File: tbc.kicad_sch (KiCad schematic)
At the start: 0 parts

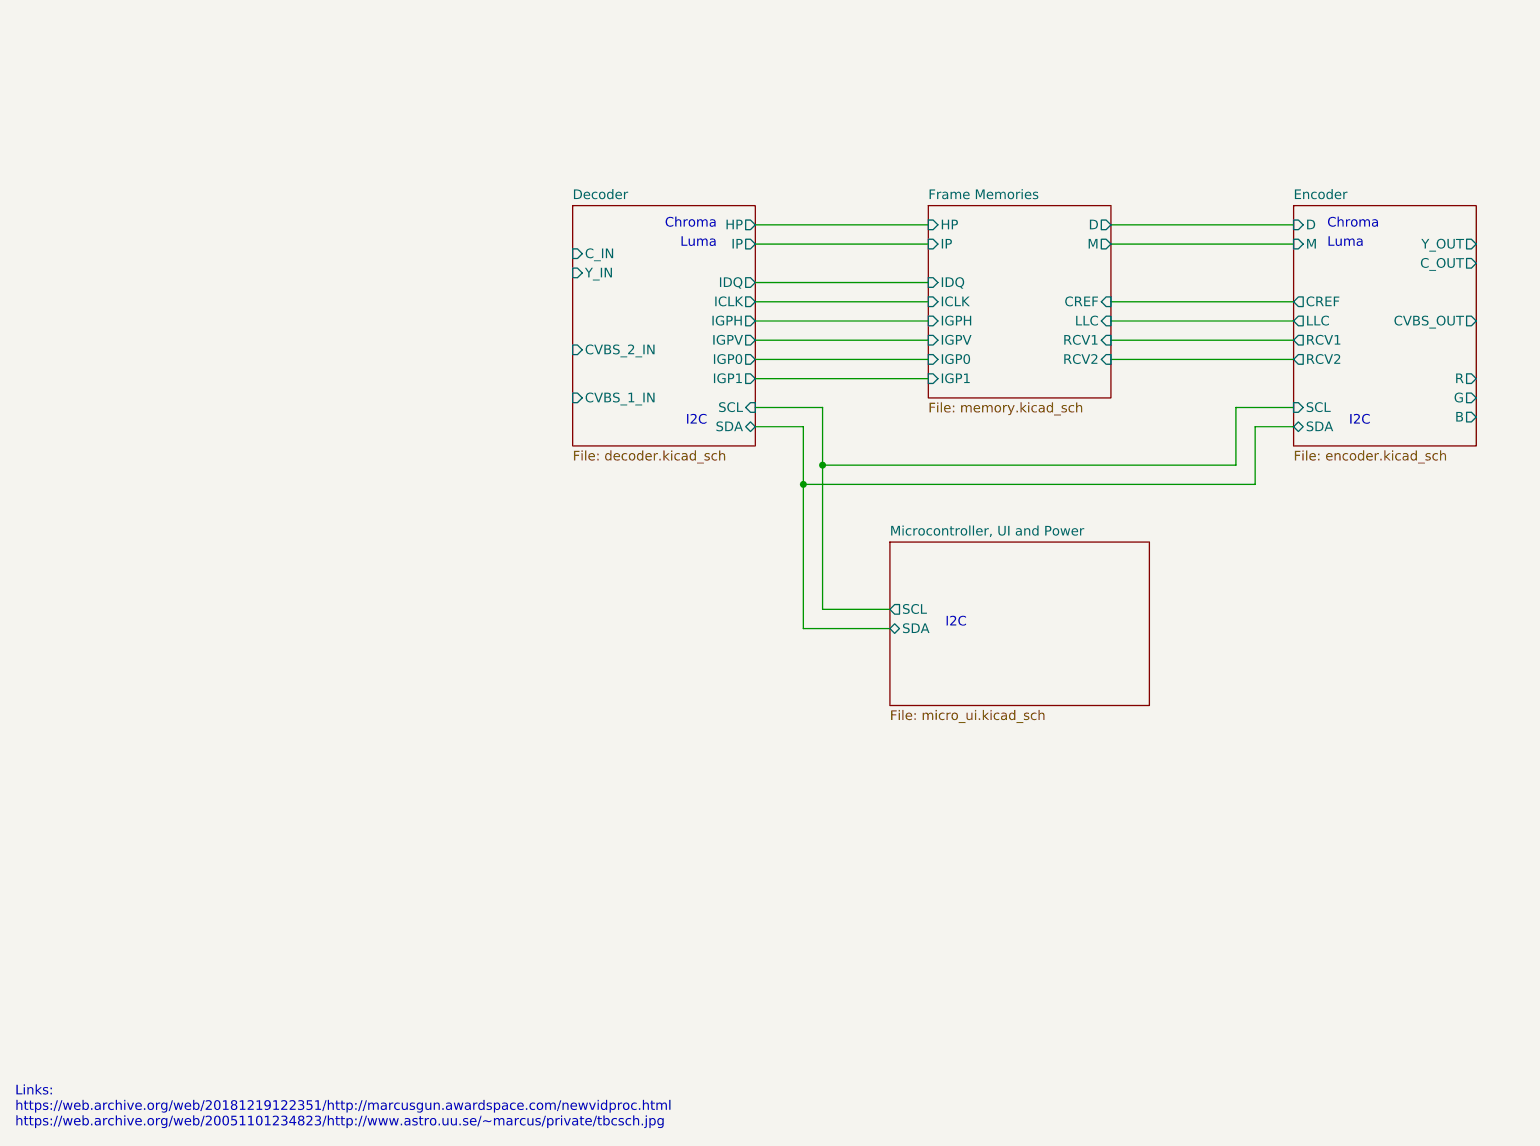
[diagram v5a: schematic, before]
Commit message: continued on schematic, added power sheet
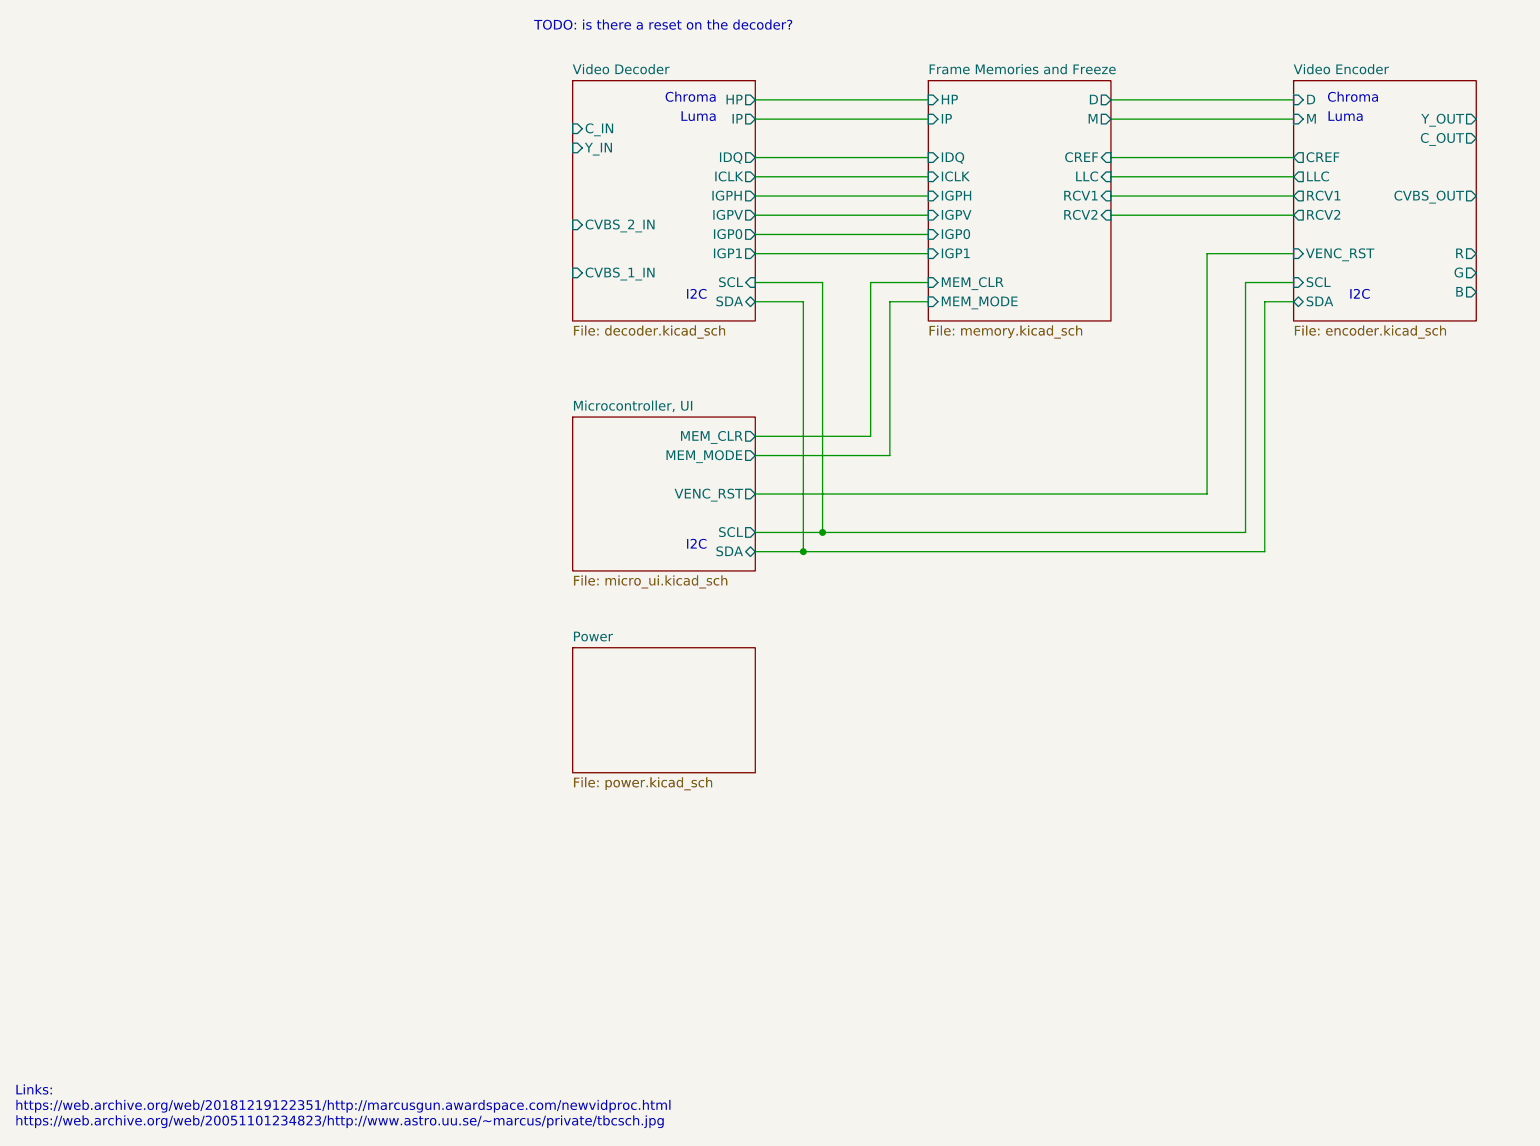
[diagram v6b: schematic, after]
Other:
- sheet Decoder renamed Video Decoder
- sheet Encoder renamed Video Encoder
- sheet Frame Memories renamed Frame Memories and Freeze
- sheet Microcontroller, UI and Power renamed Microcontroller, UI
- added sheet Power (power.kicad_sch)
- sheet Frame Memories and Freeze ports: added MEM_CLR, MEM_MODE; removed none
- sheet Microcontroller, UI ports: added MEM_CLR, MEM_MODE, VENC_RST; removed none
- sheet Video Encoder ports: added VENC_RST; removed none
- note added: "TODO: is there a reset on the decoder?"

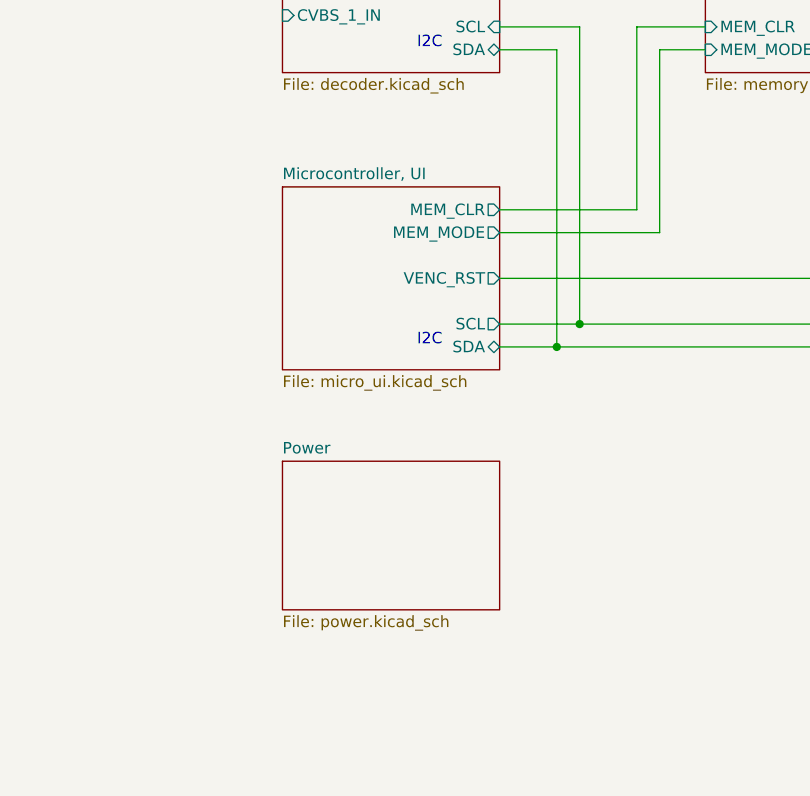
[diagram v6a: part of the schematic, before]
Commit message: moved UI (2nd board) to its own project, other updates
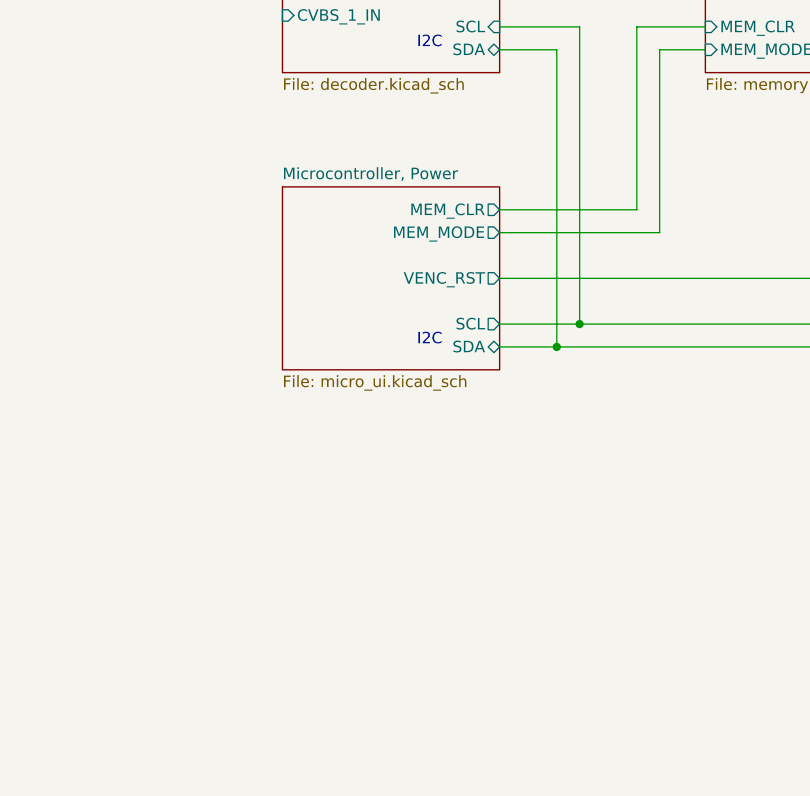
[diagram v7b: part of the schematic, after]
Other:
- sheet Microcontroller, UI renamed Microcontroller, Power
- removed sheet Power
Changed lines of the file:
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@@
     (stroke (width 0.1524) (type solid))
     (fill (color 0 0 0 0.0000))
-    (property "Sheetname" "Microcontroller, UI" (at 90.17 99.6184 0)
+    (property "Sheetname" "Microcontroller, Power" (at 90.17 99.6184 0)
       (effects (font (size 1.27 1.27)) (justify left bottom))
     )
@@
       )
     )
-  )
-  (sheet (at 90.17 130.81) (size 24.13 16.51) (fields_autoplaced)
-    (stroke (width 0.1524) (type solid))
-    (fill (color 0 0 0 0.0000))
-    (property "Sheetname" "Power" (at 90.17 130.0984 0)
-      (effects (font (size 1.27 1.27)) (justify left bottom))
-    )
-    (property "Sheetfile" "power.kicad_sch" (at 90.17 147.9046 0)
-      (effects (font (size 1.27 1.27)) (justify left top))
-    )
-    (instances
-      (project "tbc"
-        (path "/9df71e53-7941-4fd3-a17d-93619e4e3e02" (page "6"))
-      )
-    )
